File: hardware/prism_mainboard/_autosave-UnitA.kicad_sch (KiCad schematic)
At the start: 1 part, among them U1 XC7Z015-2CLG485I

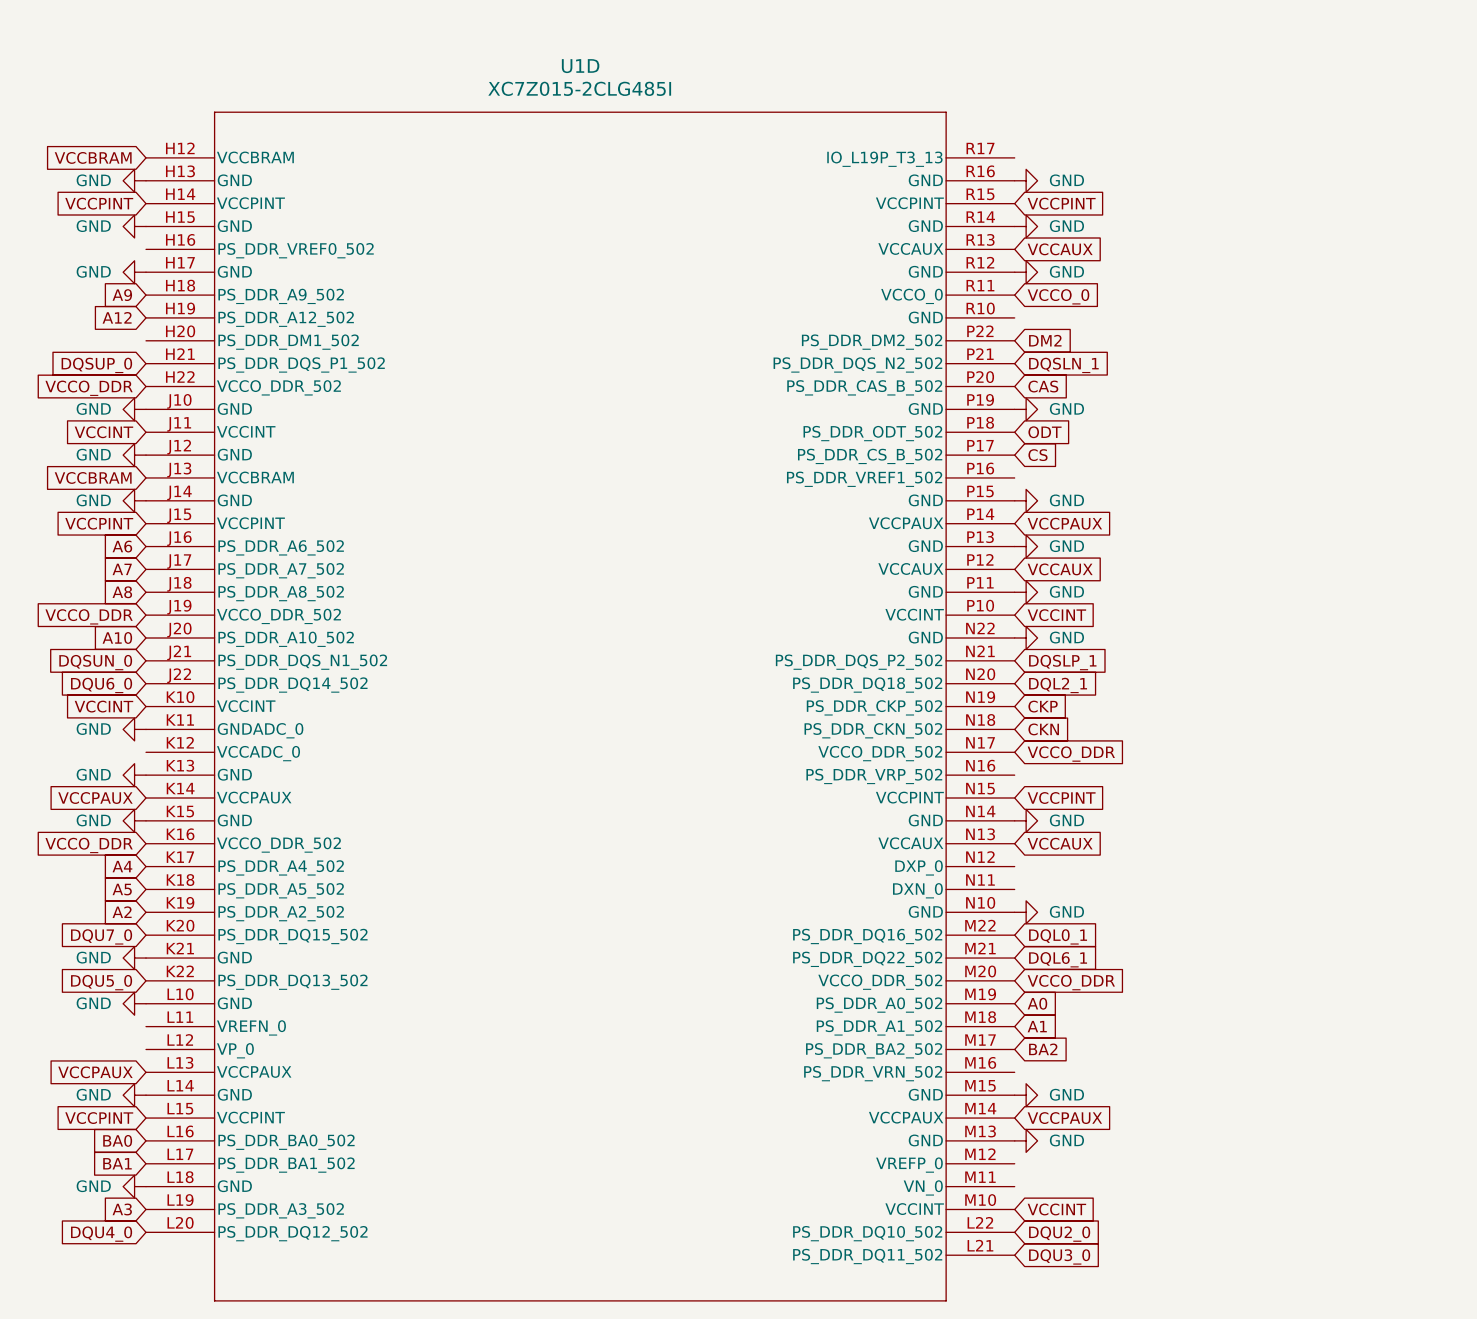
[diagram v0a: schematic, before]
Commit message: Schematic Updates & PCB Population
Populated the PCB with footprints from Main PC, should show up now. Also been updating the KiCAD schematics to connect the DDR3L Modules to the FPGA. Should be done except for a few pins that I'm not sure what they do yet. But Addressing and data pins should be connected correctly now
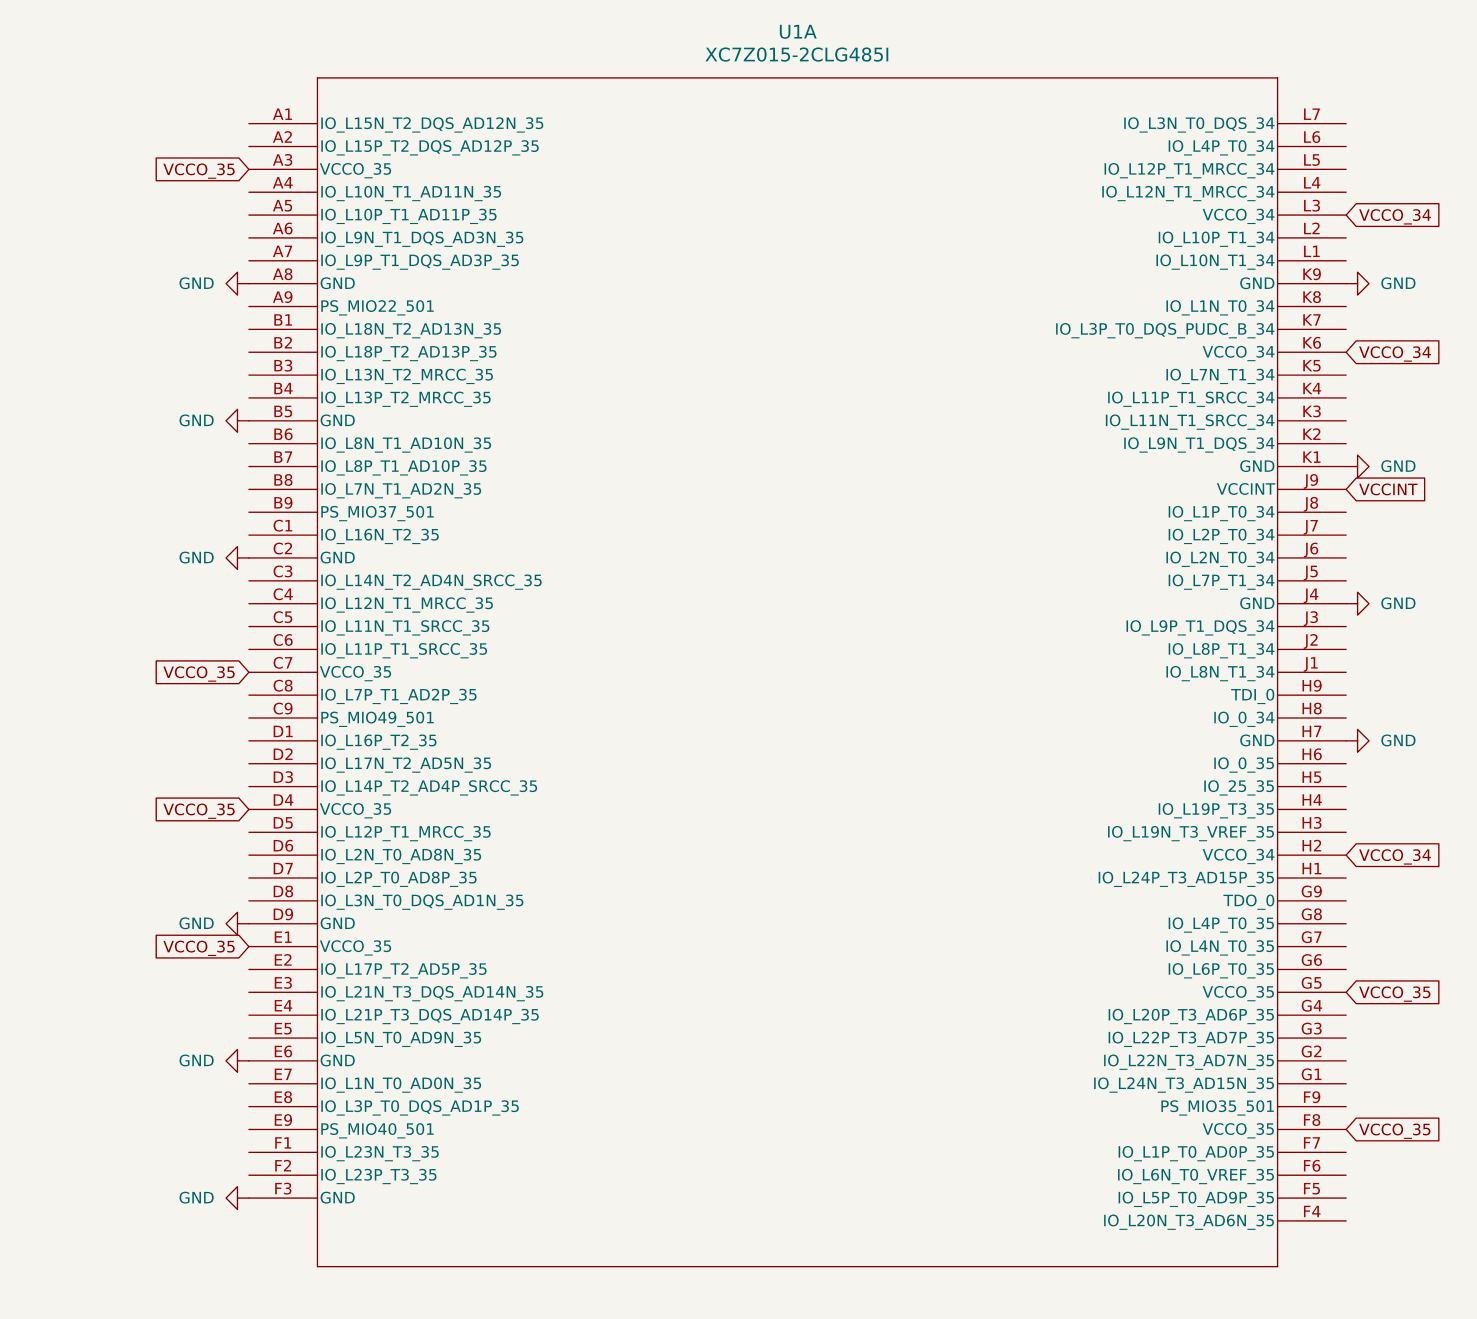
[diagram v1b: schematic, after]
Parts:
- removed U1: XC7Z015-2CLG485I, CLG485_XIL, symbol XC7Z015-CLG485:XC7Z015-2CLG485I
- added U1: XC7Z015-2CLG485I, CLG485_XIL, symbol XC7Z015-CLG485:XC7Z015-2CLG485I
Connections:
- net GND: now also U1.A8 (GND), U1.B5 (GND), U1.C2 (GND), U1.D9 (GND), U1.E6 (GND), U1.F3 (GND), U1.H7 (GND), U1.J4 (GND), U1.K1 (GND), U1.K9 (GND)
- net VCCINT: now also U1.J9 (VCCINT)
- new net VCCO_34: U1.H2 (VCCO_34), U1.K6 (VCCO_34), U1.L3 (VCCO_34)
- new net VCCO_35: U1.A3 (VCCO_35), U1.C7 (VCCO_35), U1.D4 (VCCO_35), U1.E1 (VCCO_35), U1.F8 (VCCO_35), U1.G5 (VCCO_35)
